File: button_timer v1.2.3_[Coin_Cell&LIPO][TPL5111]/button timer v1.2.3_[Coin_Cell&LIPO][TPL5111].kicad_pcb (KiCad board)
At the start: 2 copper layers, 21 x 51.6 mm, 29 parts, among them J1 Conn_01x05_Female, Q1 mmbt222, SW1 SW_Push, SW2 SW_Push, U1 TPS61097A, U2 AP2112K-3.3, U3 TPL5111, X1 ESP-12E

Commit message: Silkscreen Update
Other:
- board text added: "Button - Coin Cell v.1.2.3 TPL5111"
- board text removed: "Button - Coin Cell v.1.2"
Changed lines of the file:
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@@
     (35 F.Paste user hide)
     (36 B.SilkS user)
-    (37 F.SilkS user hide)
+    (37 F.SilkS user)
     (38 B.Mask user)
     (39 F.Mask user)
@@
     (tags "capacitor handsolder")
     (attr smd)
-    (fp_text reference C4 (at 0 -0.5 270) (layer F.SilkS)
+    (fp_text reference C4 (at 0.0626 2.9 270) (layer F.SilkS)
       (effects (font (size 0.4 0.4) (thickness 0.1)))
     )
@@
     (tags "solder jumper open")
     (attr virtual)
-    (fp_text reference JP1 (at -2.79 -0.14 180) (layer F.SilkS)
-      (effects (font (size 1 1) (thickness 0.15)))
+    (fp_text reference JP1 (at 0.05496 -1.5522 90) (layer F.SilkS)
+      (effects (font (size 0.5 0.5) (thickness 0.125)))
     )
     (fp_text value "Jumper Coin Cell" (at 0 1.9 90) (layer F.Fab)
@@
     (tags "solder jumper open")
     (attr virtual)
-    (fp_text reference JP2 (at -0.0254 -1.9558 180) (layer F.SilkS)
-      (effects (font (size 1 1) (thickness 0.15)))
+    (fp_text reference JP2 (at -2.11328 -0.21336 270) (layer F.SilkS)
+      (effects (font (size 0.5 0.5) (thickness 0.125)))
     )
     (fp_text value "Jumper LIPO" (at 0 1.9) (layer F.Fab)
@@
     (effects (font (size 2 2) (thickness 0.3) italic) (justify mirror))
   )
-  (gr_text "Button - Coin Cell v.1.2\n" (at 125.73 100.076) (layer B.SilkS)
-    (effects (font (size 0.9 0.9) (thickness 0.15)) (justify mirror))
+  (gr_text "Button - Coin Cell v.1.2.3\nTPL5111\n" (at 125.73 100.076) (layer B.SilkS)
+    (effects (font (size 0.8 0.8) (thickness 0.15)) (justify mirror))
   )
   (gr_text JLCJLCJLCJLC (at 128.905 85.725 90) (layer F.SilkS)

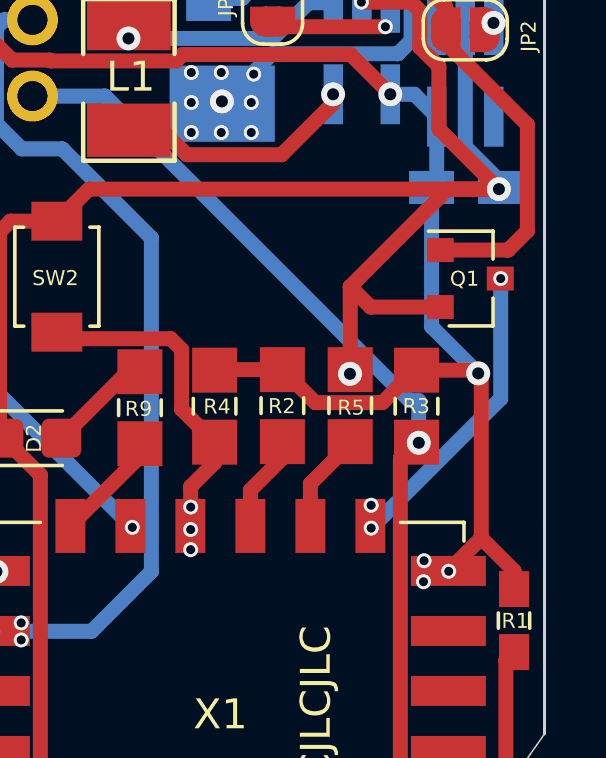
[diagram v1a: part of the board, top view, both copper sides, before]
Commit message: cap between esp vcc and ground added
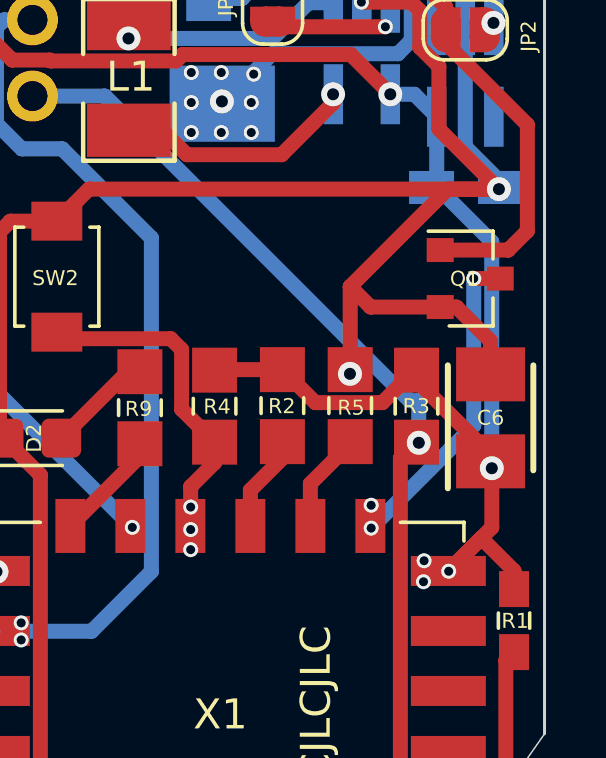
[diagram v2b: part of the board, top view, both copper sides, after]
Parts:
- added C6: TAJB476M010TNJ, SamacSys_Parts:CAPPM3528X210N, F.Cu at (134.7, 74.6)
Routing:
- net /VCC: track 54.1 -> 58.3 mm
- net /GND: track 125.5 -> 128.8 mm
- net /GND_ESP: track 10.1 -> 10.6 mm

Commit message: Added 100nF decoupling capacitors between VCC and Ground of the ESP
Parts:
- added C7: 100nF, handsolder:C_0402_1005Metric_Pad0.74x0.62mm_HandSoldermod, F.Cu at (135.3, 78.4)
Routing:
- net /GND: track 128.8 -> 135.0 mm

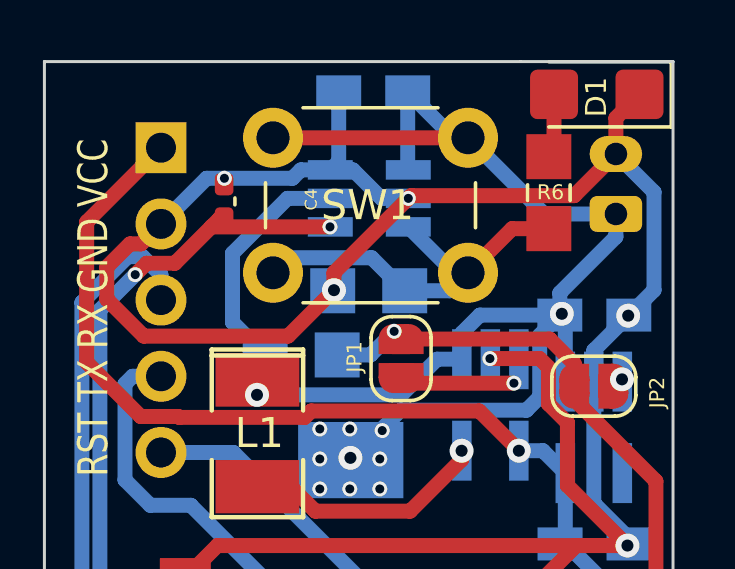
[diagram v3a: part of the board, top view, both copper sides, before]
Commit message: turned around some of the LIPO connectors
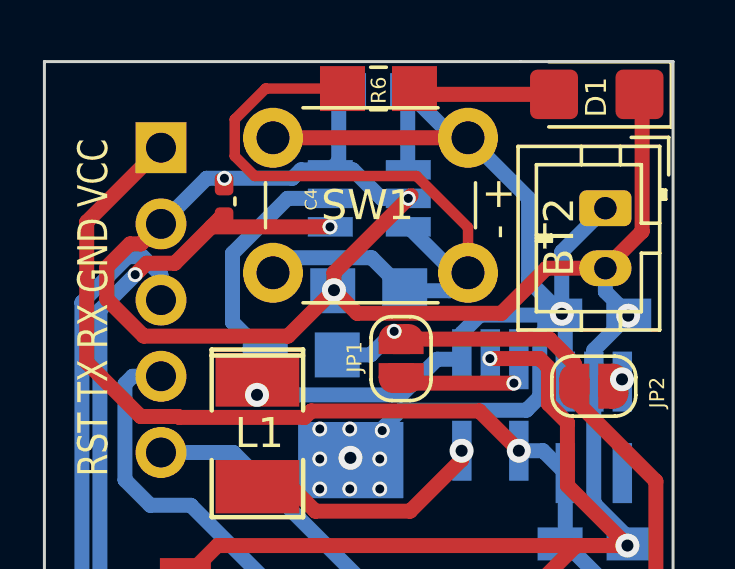
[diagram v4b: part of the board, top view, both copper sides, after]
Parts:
- BT2: moved to F.Cu
- moved R6 6.66 mm to (126.7, 51.7), turned to 180 degrees
- moved BT2 0.40 mm to (134.3, 55.7), turned to 270 degrees
- moved C5 0.18 mm to (126.7, 51.7)
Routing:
- net Net-(R6-Pad2): track 13.3 -> 25.5 mm
- net Net-(D1-Pad2): track 2.15 -> 4.73 mm
- net /GND: track 135.0 -> 137.2 mm
- net Net-(BT1-Pad1): track 46.1 -> 47.2 mm
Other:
- board text added: "- +"
- board text removed: "GND VCC"
